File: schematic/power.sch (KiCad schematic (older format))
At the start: 19 parts, among them J1 Conn_01x02, J2 Conn_01x02, J3 Conn_01x02, J4 Conn_01x02, J5 Conn_02x06_Odd_Even, J6 Conn_01x02, J7 Conn_01x02, J8 Conn_02x06_Odd_Even, SW1 SW_DIP_x01, U1 LM2595S-3.3

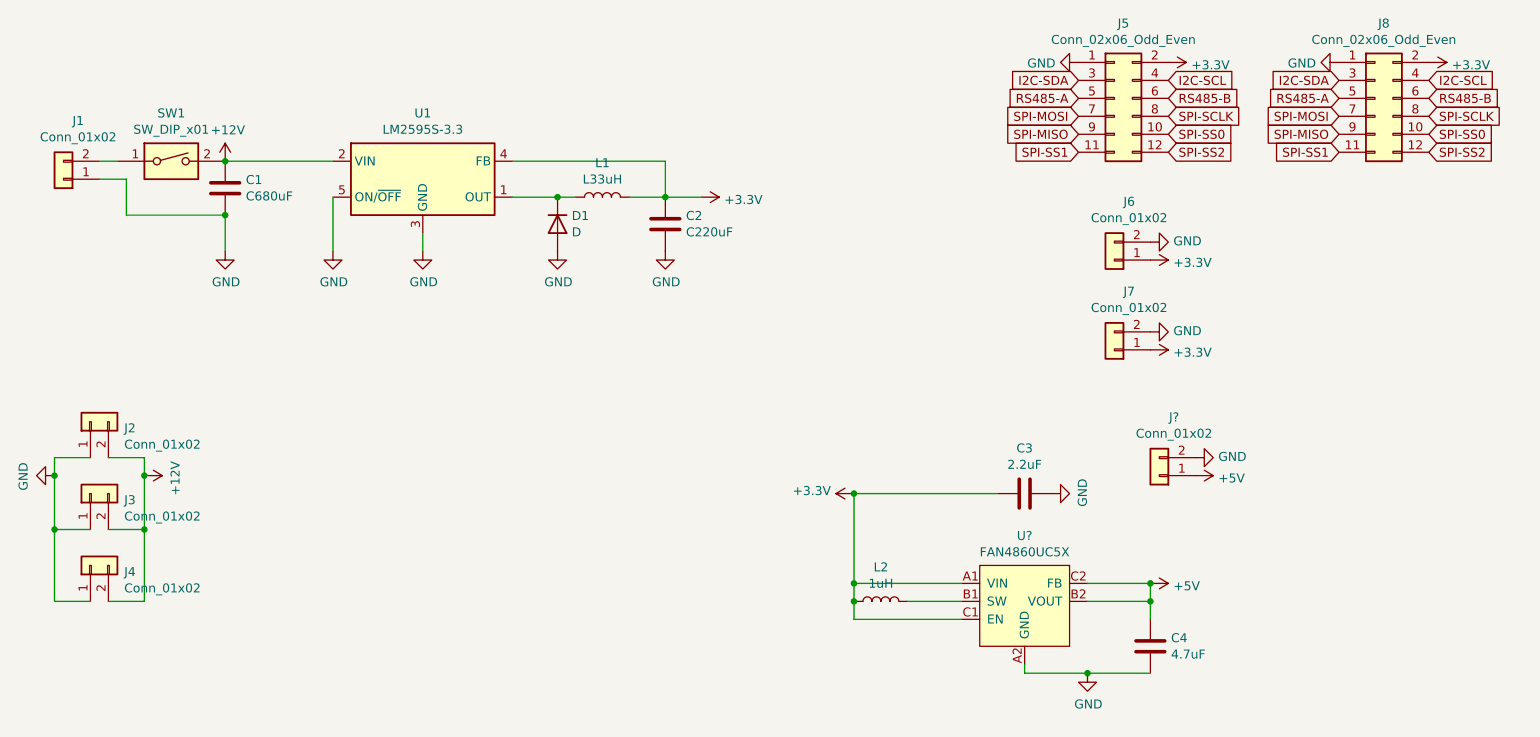
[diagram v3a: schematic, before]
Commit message: boost converter on Apsu board and PCB design
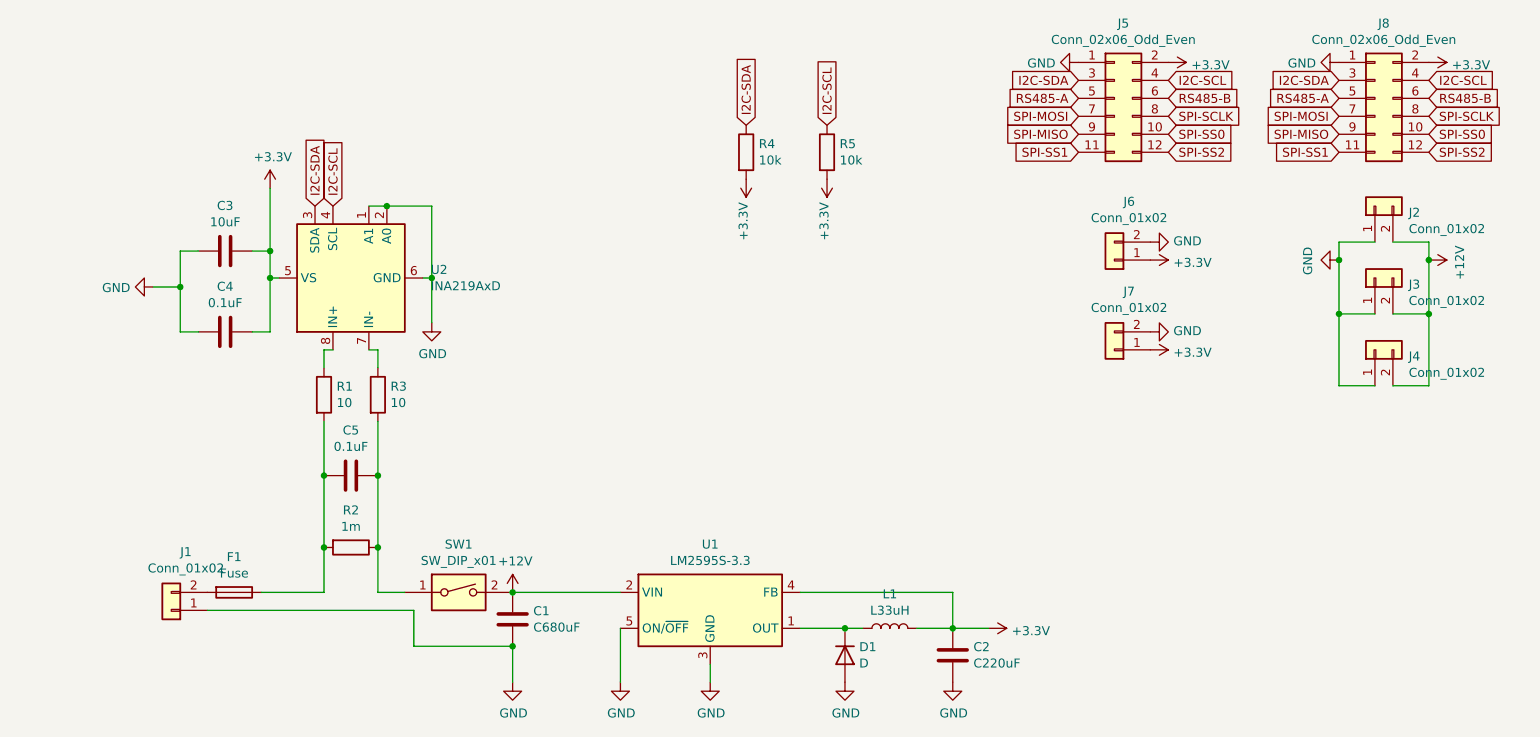
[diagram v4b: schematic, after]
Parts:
- removed J?: Conn_01x02, Connector_JST:JST_XH_B2B-XH-A_1x02_P2.50mm_Vertical, symbol Connector_Generic:Conn_01x02
- removed L2: 1uH, symbol Device:L
- removed U?: FAN4860UC5X, Package_CSP:WLCSP-6_1.4x1.0mm_P0.4mm, symbol Apsu_Library:FAN4860UC5X
- added C5: 0.1uF, Capacitor_SMD:C_0805_2012Metric_Pad1.15x1.40mm_HandSolder, symbol Device:C
- added F1: Fuse, Fuse:Fuseholder_Cylinder-5x20mm_Schurter_0031_8201_Horizontal_Open, symbol Device:Fuse
- added R1, R3: 10, Resistor_SMD:R_0805_2012Metric_Pad1.15x1.40mm_HandSolder, symbol Device:R
- added R2: 1m, Resistor_SMD:R_4020_10251Metric_Pad1.65x5.30mm_HandSolder, symbol Device:R
- added R4, R5: 10k, Resistor_SMD:R_0805_2012Metric_Pad1.15x1.40mm_HandSolder, symbol Device:R
- added U2: INA219AxD, Package_SO:SOIC-8_3.9x4.9mm_P1.27mm, symbol Analog_ADC:INA219AxD
- C3: value 2.2uF -> 10uF; footprint (none) -> Capacitor_SMD:C_0805_2012Metric_Pad1.15x1.40mm_HandSolder
- C4: value 4.7uF -> 0.1uF; footprint (none) -> Capacitor_SMD:C_0805_2012Metric_Pad1.15x1.40mm_HandSolder
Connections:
- net +5V is gone; now on net +3V3: C4.1
- net +3V3: now also C3.1, R4.2, R5.2, U2.5 (VS); no longer C3.2
- net GND: now also C3.2, U2.1 (A1), U2.2 (A0), U2.6 (GND); no longer C3.1
- net I2C-SCL: now also R5.1, U2.4 (SCL)
- net I2C-SDA: now also R4.1, U2.3 (SDA)
- net at J1.2 (Pin_2): now also F1.2; no longer SW1.1
- new net: C5.1, R2.1, R3.2, SW1.1
- new net: C5.2, F1.1, R1.2, R2.2
- new net: R3.1, U2.7 (IN-)
- new net: R1.1, U2.8 (IN+)
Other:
- moved on the sheet: C1, C2, D1, J1, J2, J3, J4, L1, SW1, U1

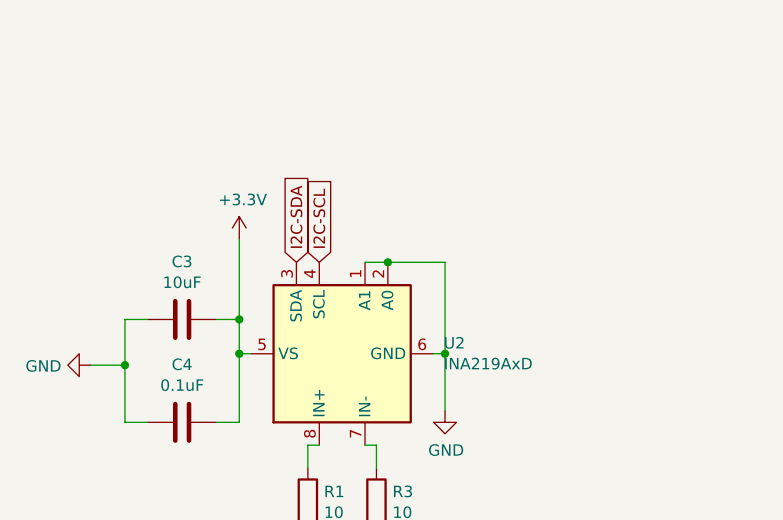
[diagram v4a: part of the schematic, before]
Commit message: JTAG anti-ring resistors
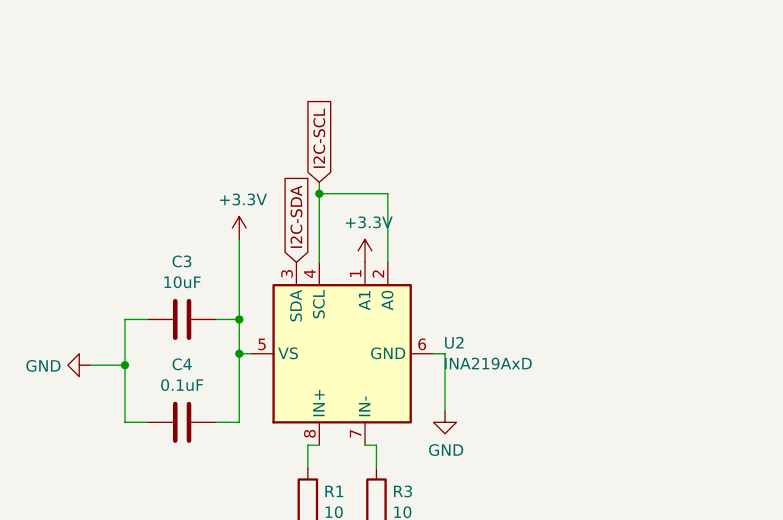
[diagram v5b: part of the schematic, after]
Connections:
- net +3V3: now also U2.1 (A1)
- net GND: no longer U2.1 (A1), U2.2 (A0)
- net I2C-SCL: now also U2.2 (A0)

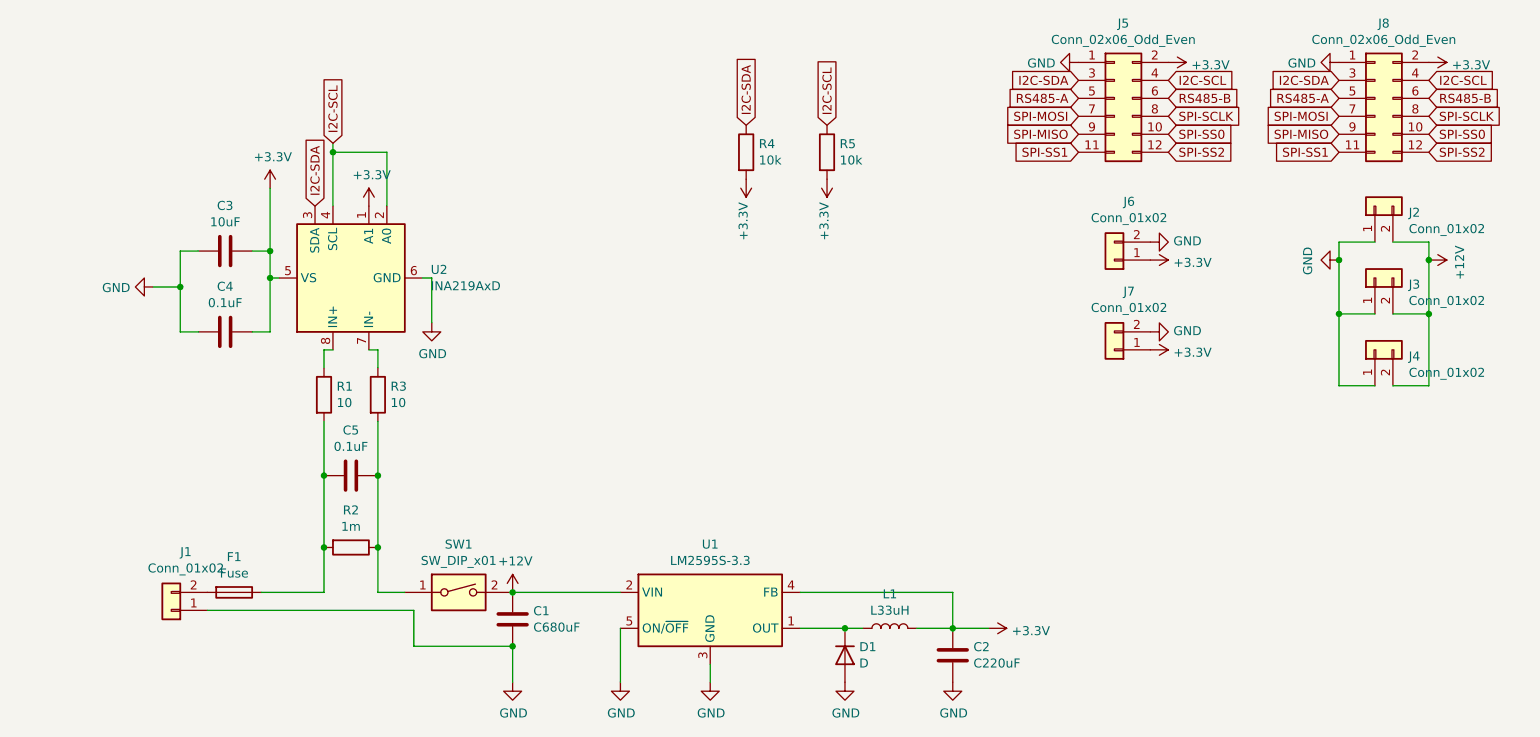
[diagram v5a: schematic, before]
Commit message: added extra resistor, removed unnessesary components and added traces to power board
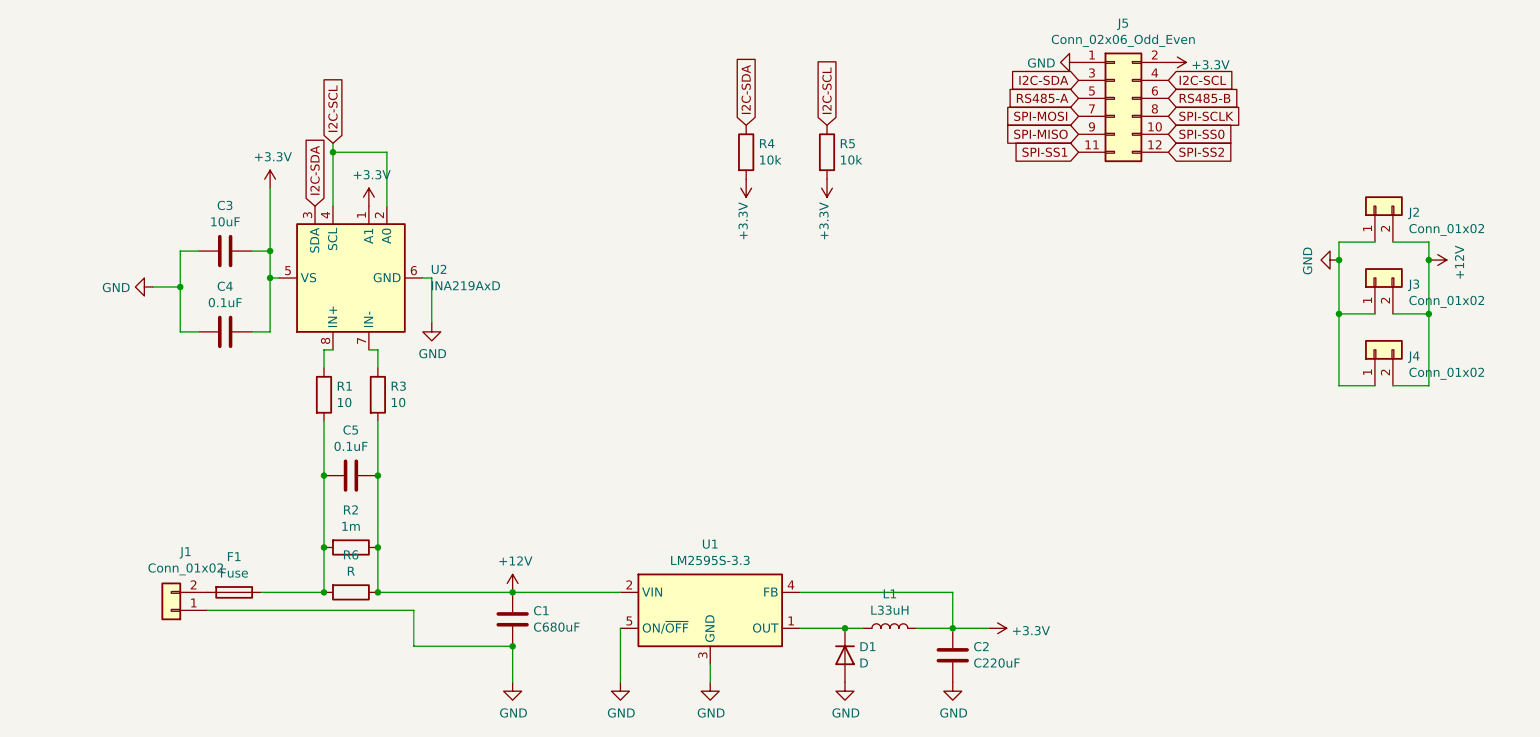
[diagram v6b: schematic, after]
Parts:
- removed J6, J7: Conn_01x02, Connector_JST:JST_XH_B2B-XH-A_1x02_P2.50mm_Vertical, symbol Connector_Generic:Conn_01x02
- removed J8: Conn_02x06_Odd_Even, Connector_IDC:IDC-Header_2x06_P2.54mm_Vertical, symbol Connector_Generic:Conn_02x06_Odd_Even
- removed SW1: SW_DIP_x01, Button_Switch_THT:SW_MEC_5GTH9, symbol Switch:SW_DIP_x01
- added R6: R, Resistor_THT:R_Axial_DIN0207_L6.3mm_D2.5mm_P10.16mm_Horizontal, symbol Device:R
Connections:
- net +12V: now also C5.1, R2.1, R3.2, R6.1
- net at C5.2, F1.1, R1.2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: now also R6.2
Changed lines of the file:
@@
-$EndComp
-$Comp
-L Switch:SW_DIP_x01 SW1
-U 1 1 5EEDDF64
-P 3850 4250
-AR Path="/5EEDDF64" Ref="SW1"  Part="1"
-AR Path="/5EEC6D97/5EEDDF64" Ref="SW1"  Part="1"
-F 0 "SW1" H 3850 4517 50  0000 C CNN
-F 1 "SW_DIP_x01" H 3850 4426 50  0000 C CNN
-F 2 "Button_Switch_THT:SW_MEC_5GTH9" H 3850 4250 50  0001 C CNN
-F 3 "~" H 3850 4250 50  0001 C CNN
-	1    3850 4250
-	1    0    0    -1
 $EndComp
 $Comp
@@
 F 3 "" H 7800 1300 50  0001 C CNN
 	1    7800 1300
-	0    1    1    0
-$EndComp
-$Comp
-L Connector_Generic:Conn_01x02 J6
-U 1 1 5EEAAB7C
-P 7500 2400
-F 0 "J6" H 7418 2075 50  0000 C CNN
-F 1 "Conn_01x02" H 7418 2166 50  0000 C CNN
-F 2 "Connector_JST:JST_XH_B2B-XH-A_1x02_P2.50mm_Vertical" H 7500 2400 50  0001 C CNN
-F 3 "~" H 7500 2400 50  0001 C CNN
-	1    7500 2400
-	-1   0    0    1
-$EndComp
-$Comp
-L power:GND #PWR0112
-U 1 1 5EEAC94E
-P 7700 2300
-F 0 "#PWR0112" H 7700 2050 50  0001 C CNN
-F 1 "GND" V 7705 2172 50  0000 R CNN
-F 2 "" H 7700 2300 50  0001 C CNN
-F 3 "" H 7700 2300 50  0001 C CNN
-	1    7700 2300
-	0    -1   -1   0
-$EndComp
-$Comp
-L power:+3.3V #PWR0113
-U 1 1 5EEACE9F
-P 7700 2400
-F 0 "#PWR0113" H 7700 2250 50  0001 C CNN
-F 1 "+3.3V" V 7715 2528 50  0000 L CNN
-F 2 "" H 7700 2400 50  0001 C CNN
-F 3 "" H 7700 2400 50  0001 C CNN
-	1    7700 2400
 	0    1    1    0
 $EndComp
@@
 SPI-SS2
 $Comp
-L Connector_Generic:Conn_02x06_Odd_Even J8
-U 1 1 5EEB27C4
-P 8950 1500
-F 0 "J8" H 9000 1917 50  0000 C CNN
-F 1 "Conn_02x06_Odd_Even" H 9000 1826 50  0000 C CNN
-F 2 "Connector_IDC:IDC-Header_2x06_P2.54mm_Vertical" H 8950 1500 50  0001 C CNN
-F 3 "~" H 8950 1500 50  0001 C CNN
-	1    8950 1500
-	1    0    0    -1
-$EndComp
-$Comp
-L power:GND #PWR0114
-U 1 1 5EEB27CA
-P 8750 1300
-F 0 "#PWR0114" H 8750 1050 50  0001 C CNN
-F 1 "GND" V 8755 1172 50  0000 R CNN
-F 2 "" H 8750 1300 50  0001 C CNN
-F 3 "" H 8750 1300 50  0001 C CNN
-	1    8750 1300
-	0    1    1    0
-$EndComp
-$Comp
-L power:+3.3V #PWR0115
-U 1 1 5EEB27D0
-P 9250 1300
-F 0 "#PWR0115" H 9250 1150 50  0001 C CNN
-F 1 "+3.3V" V 9265 1428 50  0000 L CNN
-F 2 "" H 9250 1300 50  0001 C CNN
-F 3 "" H 9250 1300 50  0001 C CNN
-	1    9250 1300
-	0    1    1    0
-$EndComp
-Text GLabel 8750 1400 0    50   Input ~ 0
-I2C-SDA
-Text GLabel 8750 1500 0    50   Input ~ 0
-RS485-A
-Text GLabel 8750 1600 0    50   Input ~ 0
-SPI-MOSI
-Text GLabel 8750 1700 0    50   Input ~ 0
-SPI-MISO
-Text GLabel 8750 1800 0    50   Input ~ 0
-SPI-SS1
-Text GLabel 9250 1400 2    50   Input ~ 0
-I2C-SCL
-Text GLabel 9250 1500 2    50   Input ~ 0
-RS485-B
-Text GLabel 9250 1600 2    50   Input ~ 0
-SPI-SCLK
-Text GLabel 9250 1700 2    50   Input ~ 0
-SPI-SS0
-Text GLabel 9250 1800 2    50   Input ~ 0
-SPI-SS2
-$Comp
-L power:GND #PWR0116
-U 1 1 5EEB410E
-P 7700 2800
-F 0 "#PWR0116" H 7700 2550 50  0001 C CNN
-F 1 "GND" V 7705 2672 50  0000 R CNN
-F 2 "" H 7700 2800 50  0001 C CNN
-F 3 "" H 7700 2800 50  0001 C CNN
-	1    7700 2800
-	0    -1   -1   0
-$EndComp
-$Comp
-L power:+3.3V #PWR0117
-U 1 1 5EEB4114
-P 7700 2900
-F 0 "#PWR0117" H 7700 2750 50  0001 C CNN
-F 1 "+3.3V" V 7715 3028 50  0000 L CNN
-F 2 "" H 7700 2900 50  0001 C CNN
-F 3 "" H 7700 2900 50  0001 C CNN
-	1    7700 2900
-	0    1    1    0
-$EndComp
-$Comp
-L Connector_Generic:Conn_01x02 J7
-U 1 1 5EEB4108
-P 7500 2900
-F 0 "J7" H 7418 2575 50  0000 C CNN
-F 1 "Conn_01x02" H 7418 2666 50  0000 C CNN
-F 2 "Connector_JST:JST_XH_B2B-XH-A_1x02_P2.50mm_Vertical" H 7500 2900 50  0001 C CNN
-F 3 "~" H 7500 2900 50  0001 C CNN
-	1    7500 2900
-	-1   0    0    1
-$EndComp
-$Comp
 L Device:Fuse F1
 U 1 1 5EEFCFCC
@@
 Wire Wire Line
 	3400 4000 3400 4250
-Wire Wire Line
-	3400 4250 3550 4250
 Connection ~ 3400 4000
 Wire Wire Line
@@
 $EndComp
 $Comp
-L power:+3.3V #PWR?
+L power:+3.3V #PWR0123
 U 1 1 5EFBA46A
 P 3350 2100
-F 0 "#PWR?" H 3350 1950 50  0001 C CNN
+F 0 "#PWR0123" H 3350 1950 50  0001 C CNN
 F 1 "+3.3V" H 3365 2273 50  0000 C CNN
 F 2 "" H 3350 2100 50  0001 C CNN
@@
 Wire Wire Line
 	3150 1800 3150 1750
+$Comp
+L Device:R R6
+U 1 1 5F06EAD5
+P 3250 4250
+F 0 "R6" V 3043 4250 50  0000 C CNN
+F 1 "R" V 3134 4250 50  0000 C CNN
+F 2 "Resistor_THT:R_Axial_DIN0207_L6.3mm_D2.5mm_P10.16mm_Horizontal" V 3180 4250 50  0001 C CNN
+F 3 "~" H 3250 4250 50  0001 C CNN
+	1    3250 4250
+	0    1    1    0
+$EndComp
+Connection ~ 3400 4250
+Connection ~ 3100 4250
+Wire Wire Line
+	3400 4250 4150 4250
 $EndSCHEMATC
